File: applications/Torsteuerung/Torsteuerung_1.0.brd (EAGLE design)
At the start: 86.3 x 67.3 mm, 77 parts, among them IC1 74HC14N, IC2 74HC14N

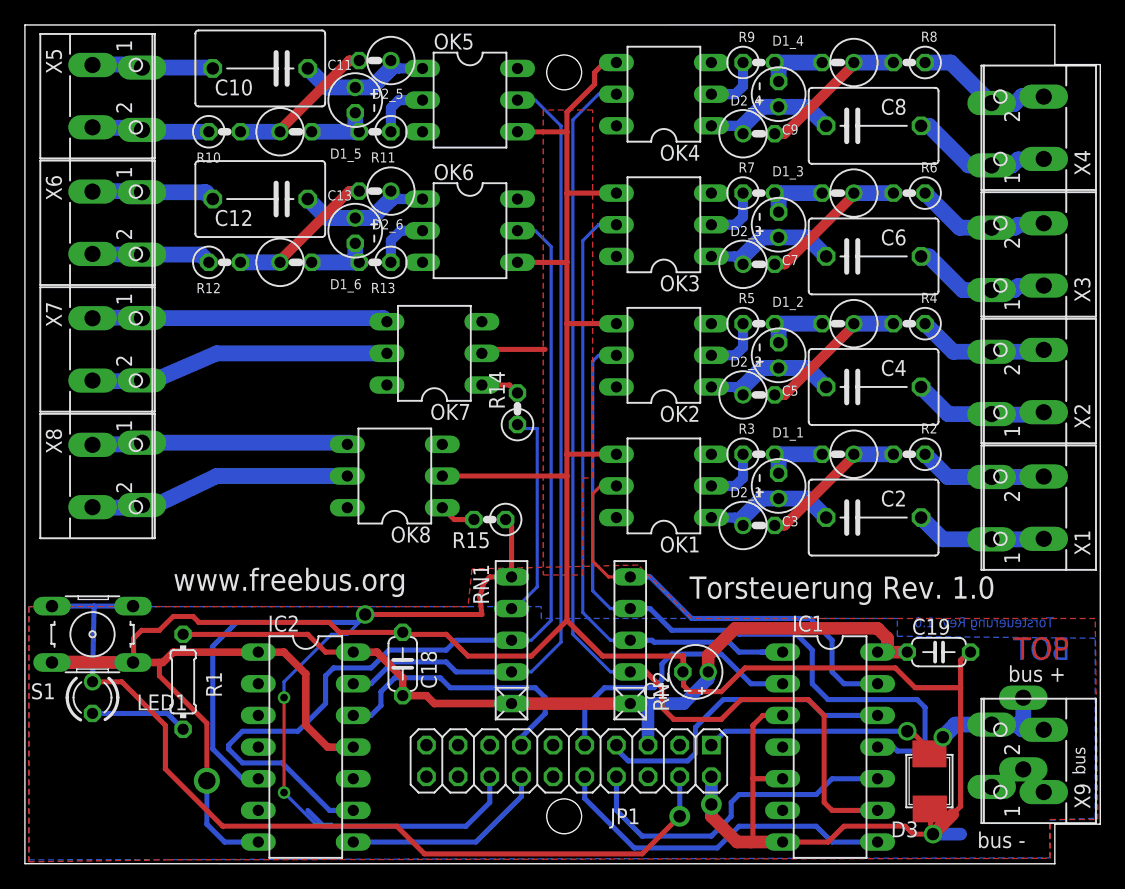
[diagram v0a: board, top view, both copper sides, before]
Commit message: Tasterschnittstelle_DIL übersiedelte nach UPModule
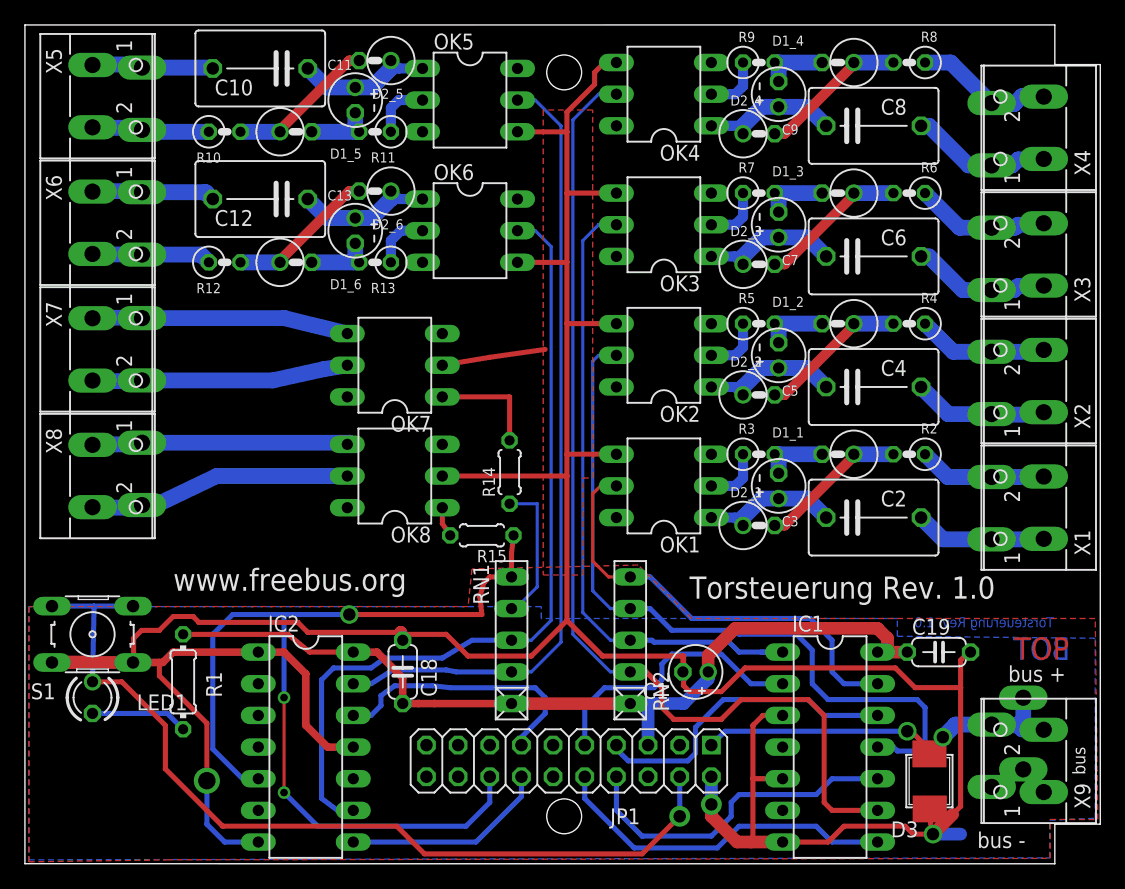
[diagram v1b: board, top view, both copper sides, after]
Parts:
- R14, R15: device rcl:0207/2V -> rcl:0204/5
- moved R14 5.12 mm to (38.4, 30.8)
- moved OK7 3.31 mm to (29.2, 39.4)
- moved R15 1.42 mm to (36.2, 25.7)
- moved C18 0.63 mm to (29.8, 14.8)
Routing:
- net N$19: track 76.9 -> 65.7 mm
- net IO8: track 84.8 -> 77.9 mm
- net N$22: track 3.12 -> 8.89 mm
- net IO7: track 17.1 -> 11.6 mm
- net GND: track 271.1 -> 275.0 mm
- net N$11: track 24.1 -> 20.6 mm
- net N$15: track 23.8 -> 20.6 mm
- net IO5: track 22.6 -> 21.7 mm
- net N$18: track 64.5 -> 63.8 mm
- net N$21: track 2.93 -> 2.41 mm
